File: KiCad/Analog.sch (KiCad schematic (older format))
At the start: 28 parts, among them U34 LM358, U35 74LVC1G125, U4 40245

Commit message: Schematic Update First Draft, ERC Passed
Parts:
- removed U4: 40245, Package_SO:TSSOP-20_4.4x6.5mm_P0.65mm, symbol 4xxx_IEEE:40245
- added U4: 74HC245, Package_SO:SSOP-20_5.3x7.2mm_P0.65mm, symbol 74xx:74HC245
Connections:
- net +5V: now also U4.1 (A->B), U4.20 (VCC)
- net D0: now also U4.2 (A0)
- net D1: now also U4.3 (A1)
- net D2: now also U4.4 (A2)
- net D3: now also U4.5 (A3)
- net D4: now also U4.6 (A4)
- net D5: now also U4.7 (A5)
- net D6: now also U4.8 (A6)
- net D7: now also U4.9 (A7)
- net DAC/D0: now also U4.18 (B0)
- net DAC/D1: now also U4.17 (B1)
- net DAC/D2: now also U4.16 (B2)
- net DAC/D3: now also U4.15 (B3)
- net DAC/D4: now also U4.14 (B4)
- net DAC/D5: now also U4.13 (B5)
- net DAC/D6: now also U4.12 (B6)
- net DAC/D7: now also U4.11 (B7)
- net GND: now also U4.10 (GND), U4.19 (CE)
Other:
- note added: "R2R DAC generates the reference voltage dictated by\nthe SA Register and Statemachine. This voltage is then \ncompared to the input voltage."
- moved on the sheet: C33, C34, C35, C36, D19, D20, D21, D22, D23, D24, D25, D26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

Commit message: First part placement
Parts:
- D19, D20, D21, D22, D23, D24, D25, D26, D27: footprint LED_SMD:LED_0805_2012Metric -> LED_SMD:LED_0603_1608Metric
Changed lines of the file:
@@
 F 0 "D19" H 3250 3200 50  0000 C CNN
 F 1 "LED_Small" H 2900 3200 50  0000 C CNN
-F 2 "LED_SMD:LED_0805_2012Metric" V 3150 3250 50  0001 C CNN
+F 2 "LED_SMD:LED_0603_1608Metric" V 3150 3250 50  0001 C CNN
 F 3 "~" V 3150 3250 50  0001 C CNN
 	1    3150 3250
@@
 F 0 "D20" H 3250 3300 50  0000 C CNN
 F 1 "LED_Small" H 2900 3300 50  0000 C CNN
-F 2 "LED_SMD:LED_0805_2012Metric" V 3150 3350 50  0001 C CNN
+F 2 "LED_SMD:LED_0603_1608Metric" V 3150 3350 50  0001 C CNN
 F 3 "~" V 3150 3350 50  0001 C CNN
 	1    3150 3350
@@
 F 0 "D21" H 3250 3400 50  0000 C CNN
 F 1 "LED_Small" H 2900 3400 50  0000 C CNN
-F 2 "LED_SMD:LED_0805_2012Metric" V 3150 3450 50  0001 C CNN
+F 2 "LED_SMD:LED_0603_1608Metric" V 3150 3450 50  0001 C CNN
 F 3 "~" V 3150 3450 50  0001 C CNN
 	1    3150 3450
@@
 F 0 "D22" H 3250 3500 50  0000 C CNN
 F 1 "LED_Small" H 2900 3500 50  0000 C CNN
-F 2 "LED_SMD:LED_0805_2012Metric" V 3150 3550 50  0001 C CNN
+F 2 "LED_SMD:LED_0603_1608Metric" V 3150 3550 50  0001 C CNN
 F 3 "~" V 3150 3550 50  0001 C CNN
 	1    3150 3550
@@
 F 0 "D23" H 3250 3600 50  0000 C CNN
 F 1 "LED_Small" H 2900 3600 50  0000 C CNN
-F 2 "LED_SMD:LED_0805_2012Metric" V 3150 3650 50  0001 C CNN
+F 2 "LED_SMD:LED_0603_1608Metric" V 3150 3650 50  0001 C CNN
 F 3 "~" V 3150 3650 50  0001 C CNN
 	1    3150 3650
@@
 F 0 "D24" H 3250 3700 50  0000 C CNN
 F 1 "LED_Small" H 2900 3700 50  0000 C CNN
-F 2 "LED_SMD:LED_0805_2012Metric" V 3150 3750 50  0001 C CNN
+F 2 "LED_SMD:LED_0603_1608Metric" V 3150 3750 50  0001 C CNN
 F 3 "~" V 3150 3750 50  0001 C CNN
 	1    3150 3750
@@
 F 0 "D25" H 3250 3800 50  0000 C CNN
 F 1 "LED_Small" H 2900 3800 50  0000 C CNN
-F 2 "LED_SMD:LED_0805_2012Metric" V 3150 3850 50  0001 C CNN
+F 2 "LED_SMD:LED_0603_1608Metric" V 3150 3850 50  0001 C CNN
 F 3 "~" V 3150 3850 50  0001 C CNN
 	1    3150 3850
@@
 F 0 "D26" H 3250 3900 50  0000 C CNN
 F 1 "LED_Small" H 2900 3900 50  0000 C CNN
-F 2 "LED_SMD:LED_0805_2012Metric" V 3150 3950 50  0001 C CNN
+F 2 "LED_SMD:LED_0603_1608Metric" V 3150 3950 50  0001 C CNN
 F 3 "~" V 3150 3950 50  0001 C CNN
 	1    3150 3950
@@
 F 0 "D27" H 9250 2900 50  0000 C CNN
 F 1 "LED_Small" H 8900 2900 50  0000 C CNN
-F 2 "LED_SMD:LED_0805_2012Metric" V 9150 2950 50  0001 C CNN
+F 2 "LED_SMD:LED_0603_1608Metric" V 9150 2950 50  0001 C CNN
 F 3 "~" V 9150 2950 50  0001 C CNN
 	1    9150 2950

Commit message: Added GND test-point
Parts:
- added TP?: GND, TestPoint:TestPoint_Keystone_5019_Minature, symbol Connector:TestPoint
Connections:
- net GND: now also TP?.1
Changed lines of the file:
@@
 Connection ~ 8700 2200
 Connection ~ 9350 3000
+$Comp
+L Connector:TestPoint TP?
+U 1 1 5EDEDF38
+P 8900 4250
+F 0 "TP?" H 8842 4276 50  0000 R CNN
+F 1 "GND" H 8842 4367 50  0000 R CNN
+F 2 "TestPoint:TestPoint_Keystone_5019_Minature" H 9100 4250 50  0001 C CNN
+F 3 "~" H 9100 4250 50  0001 C CNN
+	1    8900 4250
+	1    0    0    -1
+$EndComp
+$Comp
+L power:GND #PWR?
+U 1 1 5EDF1597
+P 8900 4350
+F 0 "#PWR?" H 8900 4100 50  0001 C CNN
+F 1 "GND" H 8905 4177 50  0000 C CNN
+F 2 "" H 8900 4350 50  0001 C CNN
+F 3 "" H 8900 4350 50  0001 C CNN
+	1    8900 4350
+	1    0    0    -1
+$EndComp
+Wire Wire Line
+	8900 4350 8900 4250
 $EndSCHEMATC

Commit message: Fixed State Numbering/Wiring Order
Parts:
- gave numbers to parts that had none: 1
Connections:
- net GND: no longer U34.6 (-)
- net at U34.7: now also U34.6 (-)
- no-connect marks 1 -> 0
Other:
- note added: "R2R DAC generates the reference voltage dictated by\nthe SA Register and state machine. This voltage is then \ncompared to the input voltage."
- note removed: "R2R DAC generates the reference voltage dictated by\nthe SA Register and Statemachine. This voltage is then \ncompared to the input voltage."
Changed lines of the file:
@@
 	1    0    0    -1
 $EndComp
-Wire Wire Line
-	7300 3100 7250 3100
-Wire Wire Line
-	7250 3100 7250 3300
-Wire Wire Line
-	7250 3300 7300 3300
-Wire Wire Line
-	7250 3300 7250 3400
-Connection ~ 7250 3300
 $Comp
 L power:GND #PWR0172
 U 1 1 5E49D036
-P 7250 3400
-F 0 "#PWR0172" H 7250 3150 50  0001 C CNN
-F 1 "GND" H 7255 3227 50  0000 C CNN
-F 2 "" H 7250 3400 50  0001 C CNN
-F 3 "" H 7250 3400 50  0001 C CNN
-	1    7250 3400
+P 7150 3150
+F 0 "#PWR0172" H 7150 2900 50  0001 C CNN
+F 1 "GND" H 7155 2977 50  0000 C CNN
+F 2 "" H 7150 3150 50  0001 C CNN
+F 3 "" H 7150 3150 50  0001 C CNN
+	1    7150 3150
 	1    0    0    -1
 $EndComp
@@
 	1    0    0    -1
 $EndComp
-NoConn ~ 7900 3200
 Text HLabel 8700 2500 2    50   Input ~ 0
 COMP_OUT
@@
 	2800 2400 2850 2400
 Text Notes 3250 5200 0    50   ~ 0
-R2R DAC generates the reference voltage dictated by\nthe SA Register and Statemachine. This voltage is then \ncompared to the input voltage.
+R2R DAC generates the reference voltage dictated by\nthe SA Register and state machine. This voltage is then \ncompared to the input voltage.
 Connection ~ 8700 2200
 Connection ~ 9350 3000
 $Comp
-L Connector:TestPoint TP?
+L Connector:TestPoint TP4
 U 1 1 5EDEDF38
 P 8900 4250
-F 0 "TP?" H 8842 4276 50  0000 R CNN
+F 0 "TP4" H 8842 4276 50  0000 R CNN
 F 1 "GND" H 8842 4367 50  0000 R CNN
 F 2 "TestPoint:TestPoint_Keystone_5019_Minature" H 9100 4250 50  0001 C CNN
@@
 $EndComp
 $Comp
-L power:GND #PWR?
+L power:GND #PWR0216
 U 1 1 5EDF1597
 P 8900 4350
-F 0 "#PWR?" H 8900 4100 50  0001 C CNN
+F 0 "#PWR0216" H 8900 4100 50  0001 C CNN
 F 1 "GND" H 8905 4177 50  0000 C CNN
 F 2 "" H 8900 4350 50  0001 C CNN
@@
 Wire Wire Line
 	8900 4350 8900 4250
+Wire Wire Line
+	7150 3100 7150 3150
+Wire Wire Line
+	7150 3100 7300 3100
+Wire Wire Line
+	7300 3300 7300 3500
+Wire Wire Line
+	7300 3500 7900 3500
+Wire Wire Line
+	7900 3500 7900 3200
 $EndSCHEMATC

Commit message: PCB v0.2.
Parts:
- D19, D20, D21, D22, D23, D24, D25, D26, D27: value LED_Small -> LED
- U34: value LM358 -> LM358ST
- U35: value 74LVC1G125 -> SN74LVC1G125DCK
- U4: value 74HC245 -> SN74HC245PWR
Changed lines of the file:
@@
 P 3150 3250
 F 0 "D19" H 3250 3200 50  0000 C CNN
-F 1 "LED_Small" H 2900 3200 50  0000 C CNN
+F 1 "LED" H 2900 3200 50  0000 C CNN
 F 2 "LED_SMD:LED_0603_1608Metric" V 3150 3250 50  0001 C CNN
 F 3 "~" V 3150 3250 50  0001 C CNN
@@
 P 3150 3350
 F 0 "D20" H 3250 3300 50  0000 C CNN
-F 1 "LED_Small" H 2900 3300 50  0000 C CNN
+F 1 "LED" H 2900 3300 50  0000 C CNN
 F 2 "LED_SMD:LED_0603_1608Metric" V 3150 3350 50  0001 C CNN
 F 3 "~" V 3150 3350 50  0001 C CNN
@@
 P 3150 3450
 F 0 "D21" H 3250 3400 50  0000 C CNN
-F 1 "LED_Small" H 2900 3400 50  0000 C CNN
+F 1 "LED" H 2900 3400 50  0000 C CNN
 F 2 "LED_SMD:LED_0603_1608Metric" V 3150 3450 50  0001 C CNN
 F 3 "~" V 3150 3450 50  0001 C CNN
@@
 P 3150 3550
 F 0 "D22" H 3250 3500 50  0000 C CNN
-F 1 "LED_Small" H 2900 3500 50  0000 C CNN
+F 1 "LED" H 2900 3500 50  0000 C CNN
 F 2 "LED_SMD:LED_0603_1608Metric" V 3150 3550 50  0001 C CNN
 F 3 "~" V 3150 3550 50  0001 C CNN
@@
 P 3150 3650
 F 0 "D23" H 3250 3600 50  0000 C CNN
-F 1 "LED_Small" H 2900 3600 50  0000 C CNN
+F 1 "LED" H 2900 3600 50  0000 C CNN
 F 2 "LED_SMD:LED_0603_1608Metric" V 3150 3650 50  0001 C CNN
 F 3 "~" V 3150 3650 50  0001 C CNN
@@
 P 3150 3750
 F 0 "D24" H 3250 3700 50  0000 C CNN
-F 1 "LED_Small" H 2900 3700 50  0000 C CNN
+F 1 "LED" H 2900 3700 50  0000 C CNN
 F 2 "LED_SMD:LED_0603_1608Metric" V 3150 3750 50  0001 C CNN
 F 3 "~" V 3150 3750 50  0001 C CNN
@@
 P 3150 3850
 F 0 "D25" H 3250 3800 50  0000 C CNN
-F 1 "LED_Small" H 2900 3800 50  0000 C CNN
+F 1 "LED" H 2900 3800 50  0000 C CNN
 F 2 "LED_SMD:LED_0603_1608Metric" V 3150 3850 50  0001 C CNN
 F 3 "~" V 3150 3850 50  0001 C CNN
@@
 P 3150 3950
 F 0 "D26" H 3250 3900 50  0000 C CNN
-F 1 "LED_Small" H 2900 3900 50  0000 C CNN
+F 1 "LED" H 2900 3900 50  0000 C CNN
 F 2 "LED_SMD:LED_0603_1608Metric" V 3150 3950 50  0001 C CNN
 F 3 "~" V 3150 3950 50  0001 C CNN
@@
 P 7600 2500
 F 0 "U34" H 7600 2867 50  0000 C CNN
-F 1 "LM358" H 7600 2776 50  0000 C CNN
+F 1 "LM358ST" H 7600 2776 50  0000 C CNN
 F 2 "Package_SO:MSOP-8_3x3mm_P0.65mm" H 7600 2500 50  0001 C CNN
 F 3 "http://www.ti.com/lit/ds/symlink/lm2904-n.pdf" H 7600 2500 50  0001 C CNN
@@
 P 7350 4300
 F 0 "U34" V 7050 4200 50  0000 L CNN
-F 1 "LM358" V 7150 4150 50  0000 L CNN
+F 1 "LM358ST" V 7150 4150 50  0000 L CNN
 F 2 "Package_SO:MSOP-8_3x3mm_P0.65mm" H 7350 4300 50  0001 C CNN
 F 3 "http://www.ti.com/lit/ds/symlink/lm2904-n.pdf" H 7350 4300 50  0001 C CNN
@@
 P 7600 3200
 F 0 "U34" H 7600 3567 50  0000 C CNN
-F 1 "LM358" H 7600 3476 50  0000 C CNN
+F 1 "LM358ST" H 7600 3476 50  0000 C CNN
 F 2 "Package_SO:MSOP-8_3x3mm_P0.65mm" H 7600 3200 50  0001 C CNN
 F 3 "http://www.ti.com/lit/ds/symlink/lm2904-n.pdf" H 7600 3200 50  0001 C CNN
@@
 P 8300 2500
 F 0 "U35" H 8450 2600 50  0000 C CNN
-F 1 "74LVC1G125" H 9000 2950 50  0000 C CNN
+F 1 "SN74LVC1G125DCK" H 9000 2950 50  0000 C CNN
 F 2 "Package_TO_SOT_SMD:SOT-353_SC-70-5" H 8300 2500 50  0001 C CNN
 F 3 "http://www.ti.com/lit/sg/scyt129e/scyt129e.pdf" H 8300 2500 50  0001 C CNN
@@
 P 9150 2950
 F 0 "D27" H 9250 2900 50  0000 C CNN
-F 1 "LED_Small" H 8900 2900 50  0000 C CNN
+F 1 "LED" H 8900 2900 50  0000 C CNN
 F 2 "LED_SMD:LED_0603_1608Metric" V 9150 2950 50  0001 C CNN
 F 3 "~" V 9150 2950 50  0001 C CNN
@@
 P 3350 1900
 F 0 "U4" H 3450 2650 50  0000 C CNN
-F 1 "74HC245" H 3550 2550 50  0000 C CNN
+F 1 "SN74HC245PWR" H 3700 2550 50  0000 C CNN
 F 2 "Package_SO:SSOP-20_5.3x7.2mm_P0.65mm" H 3350 1900 50  0001 C CNN
 F 3 "http://www.ti.com/lit/gpn/sn74HC245" H 3350 1900 50  0001 C CNN

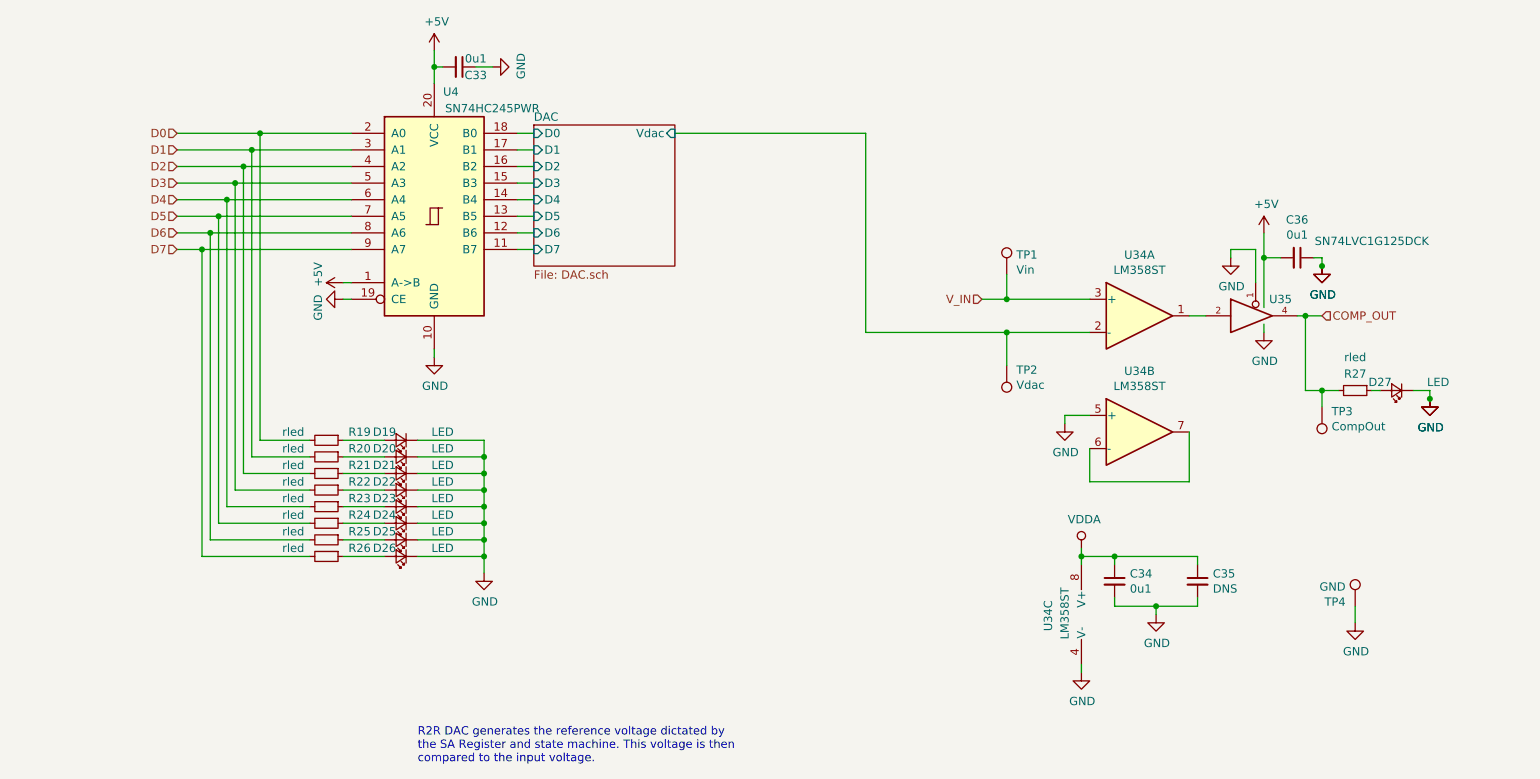
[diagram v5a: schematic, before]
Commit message: v0.3 Changed to Schmitt-Trigger ICs Added pull-down resistor to Clock Enable
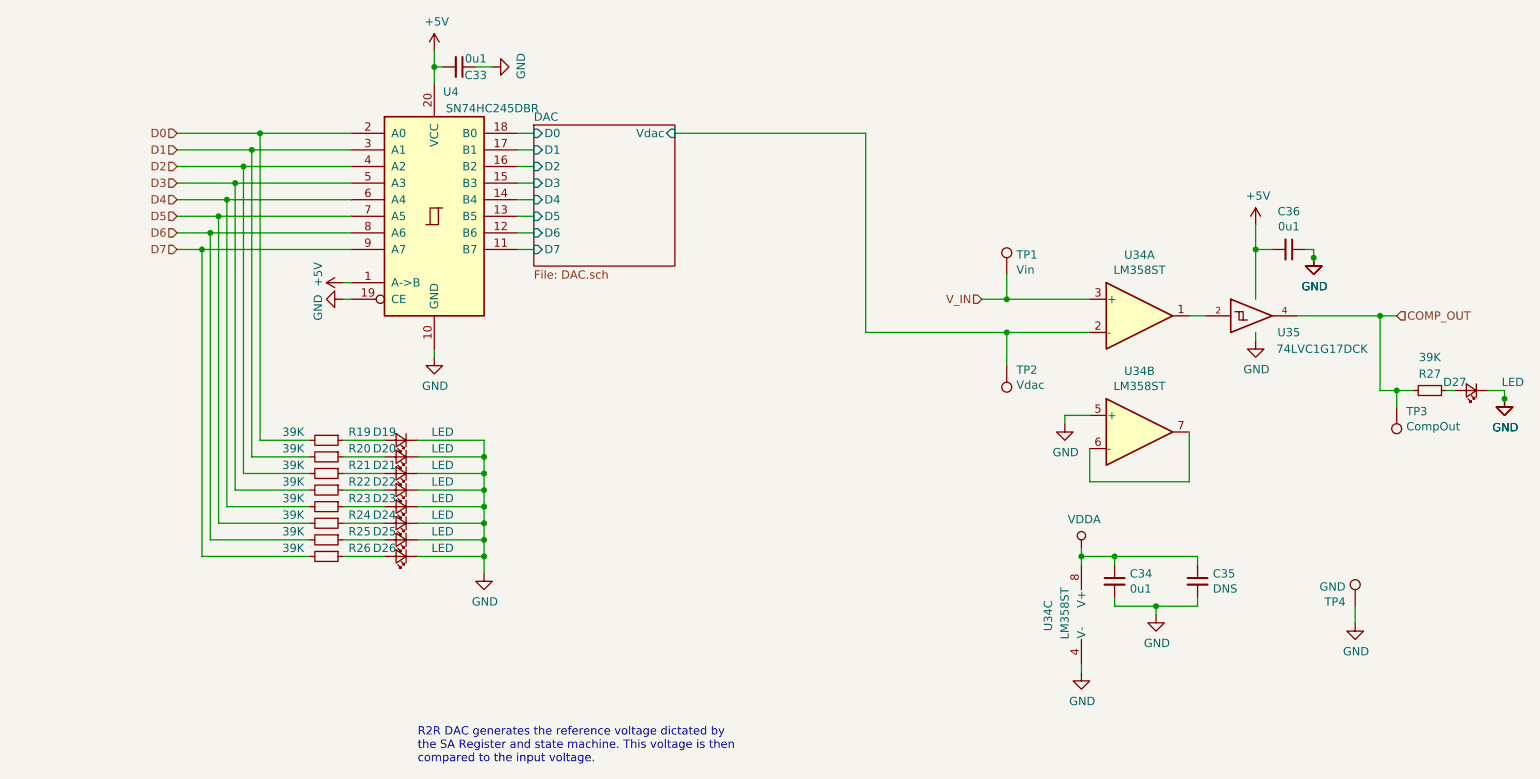
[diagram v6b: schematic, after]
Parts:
- removed U35: SN74LVC1G125DCK, Package_TO_SOT_SMD:SOT-353_SC-70-5, symbol 74xGxx:74LVC1G125
- added U35: 74LVC1G17DCK, Package_TO_SOT_SMD:SOT-353_SC-70-5, symbol 74xGxx:74LVC1G17
- R19, R20, R21, R22, R23, R24, R25, R26, R27: value rled -> 39K
- U4: value SN74HC245PWR -> SN74HC245DBR
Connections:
- net +5V: now also U35.5 (VCC)
- net COMP_OUT: now also U35.4
- net GND: now also U35.3 (GND)
- net at U34.1: now also U35.2
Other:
- moved on the sheet: C36, D27, R27, TP3
